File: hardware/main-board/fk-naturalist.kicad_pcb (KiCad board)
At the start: 2 copper layers, 91.8 x 37 mm, 131 parts, among them J1 Conn_01x07, J10 S2B-PH-SM4-TB, J11 RF-SMA-EDGE, J4 Conn_01x02, J5 Conn_01x03, J6 Conn_01x05, J7 CONN-HDR-2x5, J8 Conn_01x09, J9 MICRO-USB, M1 MOUNT_HOLE, M10 FIDUCIAL, M11 FIDUCIAL, M2 FIDUCIAL, M3 MOUNT_HOLE, M4 MOUNT_HOLE, M5 FIDUCIAL, M6 MOUNT_HOLE, M7 MICROSD, M8 FIDUCIAL, M9 FIDUCIAL, Q1 2N7002LT1G, Q2 2N7002LT1G, Q3 2N7002LT1G, Q4 2N7002LT1G, Q5 2N7002LT1G, SW1 SPNO, SW2 SPNO, U1 ATWINC1500-MR210PA, U10 FGPMMOPA6H, U103 BNO055, U11 MAX1704XX, U2 ATSAMD21G18A-AU, U4 24AA02E64, U5 S25FL116K0XMFI041, U6 BQ24074RGTT, U7 PCF8523, U8 MCP1700T-3302E/MB, U9 ISL8541x, Y1 FC-135, Y101 FC-135, Y2 FC-135

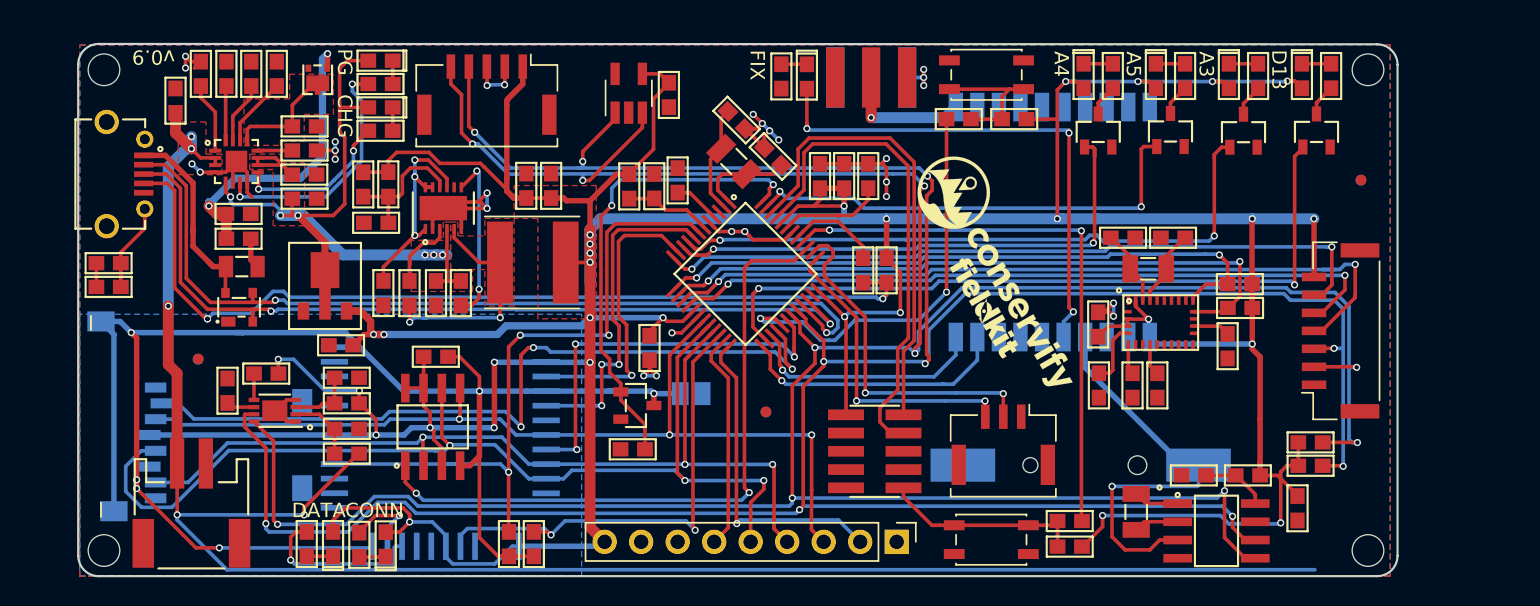
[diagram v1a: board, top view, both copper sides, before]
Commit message: Upgrade to Kicad 5. Add SK6812.
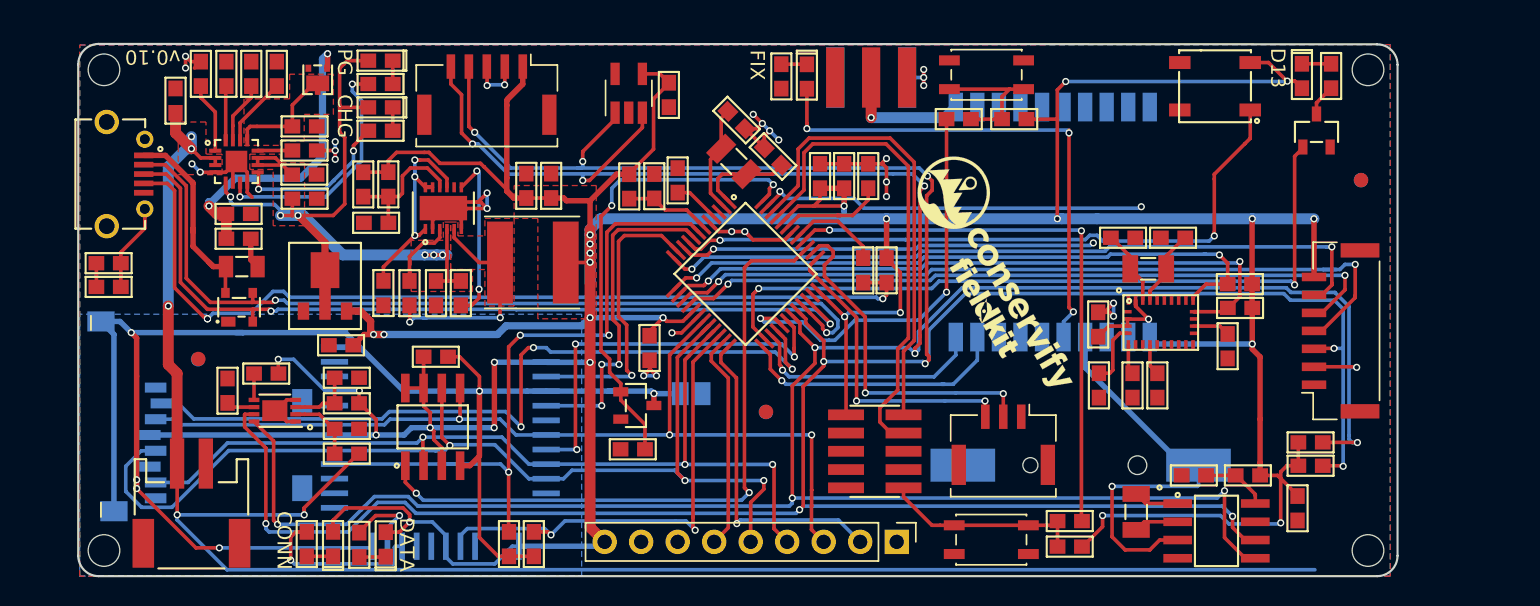
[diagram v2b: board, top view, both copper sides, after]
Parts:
- removed D4: Orange, RocketScreamKicadLibrary:LED-0603
- removed D5: Yellow, RocketScreamKicadLibrary:LED-0603
- removed D6: Blue, RocketScreamKicadLibrary:LED-0603
- removed Q2, Q3, Q4: 2N7002LT1G, RocketScreamKicadLibrary:SOT-23
- removed R18, R19, R20: 2K2, RocketScreamKicadLibrary:RES-0603
- added U3: SK6812, conservify:SK6812, F.Cu at (156.5, 112.7)
- C1, C10, C105, C106, C107, C108, C11, C12, C14, C18, C19, C20, C21, C22, C23, C24, C25, C26, C27, C28, C29, C3, C30, C31, C32, C4, C5, C6, C7, C8, C9: footprint RocketScreamKicadLibrary:CAP-0603 -> conservify:CAP-0603
- D1, D10, D11, D2, D3, D9: footprint RocketScreamKicadLibrary:LED-0603 -> conservify:LED-0603
- D7: footprint RocketScreamKicadLibrary:SOT-1016 -> conservify:SOT-1016
- D8: footprint RocketScreamKicadLibrary:SOT-143B -> conservify:SOT-143B
- F1: footprint RocketScreamKicadLibrary:MF-PSMF020X -> conservify:MF-PSMF020X
- J10: footprint RocketScreamKicadLibrary:S2B-PH-SM4-TB -> conservify:S2B-PH-SM4-TB
- J11: footprint RocketScreamKicadLibrary:RF-SMA-EDGE -> conservify:RF-SMA-EDGE
- J8: footprint Socket_Strips:Socket_Strip_Straight_1x09_Pitch2.54mm -> conservify:Socket_Strip_Straight_1x09_Pitch2.54mm
- L1, L2: footprint RocketScreamKicadLibrary:IND-0603 -> conservify:IND-0603
- M1, M3, M4, M6: footprint RocketScreamKicadLibrary:HOLE_NPTH_2.2MM -> conservify:HOLE_NPTH_2.2MM
- M10, M11, M2, M5, M8, M9: footprint Fiducials:Fiducial_0.75mm_Dia_1.5mm_Outer -> conservify:FIDUCIAL-1MM
- Q1, Q5: footprint RocketScreamKicadLibrary:SOT-23 -> conservify:SOT-23
- R1, R10, R101, R102, R103, R17, R2, R21, R22, R23, R24, R25, R26, R27, R3, R30, R31, R32, R33, R34, R35, R36, R37, R38, R39, R4, R40, R41, R42, R43, R44, R45, R5, R6, R8, R9: footprint RocketScreamKicadLibrary:RES-0603 -> conservify:RES-0603
- U11: footprint Housings_DFN_QFN:DFN-8-1EP_3x2mm_Pitch0.5mm -> conservify:DFN-8-1EP_3x2mm_Pitch0.5mm
- U2: footprint RocketScreamKicadLibrary:TQFP-48_7x7mm_Pitch0.5mm -> conservify:TQFP-48_7x7mm_Pitch0.5mm
- U4: footprint TO_SOT_Packages_SMD:SOT-23-5_HandSoldering -> conservify:SOT-23-5_HandSoldering
- U5, U7: footprint RocketScreamKicadLibrary:SOIC-8-N -> conservify:SOIC-8-N
- U6: footprint RocketScreamKicadLibrary:QFN-16_3x3mm -> conservify:QFN-16_3x3mm
- U8: footprint RocketScreamKicadLibrary:SOT-89 -> conservify:SOT-89
- U9: footprint Housings_DFN_QFN:DFN-12-1EP_3x4mm_Pitch0.5mm -> conservify:DFN-12-1EP_3x4mm_Pitch0.5mm
- Y1, Y101, Y2: footprint RocketScreamKicadLibrary:ABS07 -> conservify:ABS07
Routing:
- net /A4: track 36.9 -> 29.2 mm
- net /A5: track 32.3 -> 27.1 mm
- net /A3: track 44.4 -> 47.3 mm
- net Net-(Q2-Pad3): track 2.23 -> 0.00 mm
- net Net-(Q3-Pad3): track 2.21 -> 0.00 mm
- net Net-(Q4-Pad3): track 2.18 -> 0.00 mm
- net Net-(D6-Pad1): track 2.03 -> 0.00 mm
- net Net-(D5-Pad1): track 2.03 -> 0.00 mm
- net Net-(D4-Pad1): track 2.03 -> 0.00 mm
- net 3V3: track 365.4 -> 364.2 mm, vias 31 -> 29
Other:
- board text added: "v0.10"
- board text removed: "A3"
- board text removed: "A4"
- board text removed: "A5"
- board text removed: "v0.9"

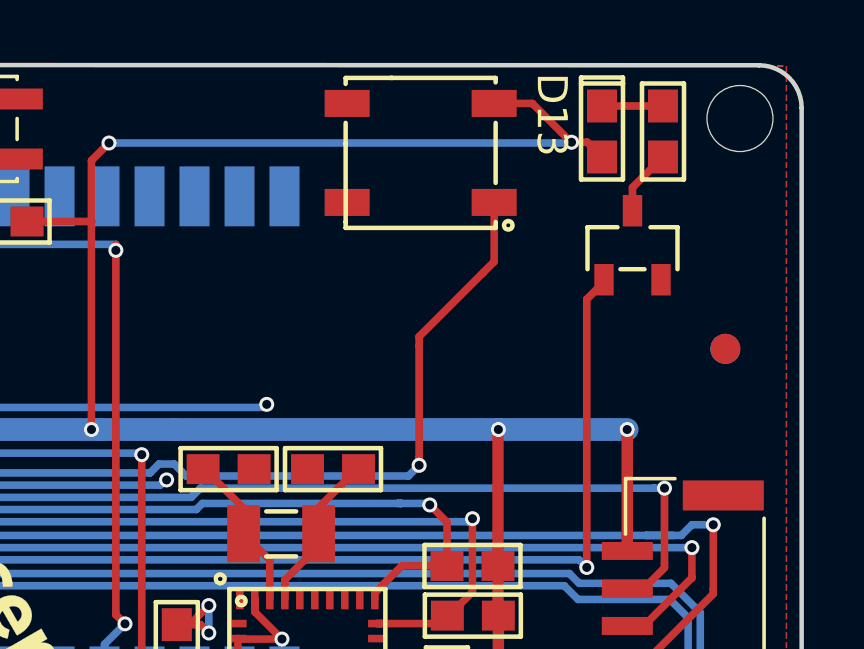
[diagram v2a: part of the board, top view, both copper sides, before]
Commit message: Fix SK6812.
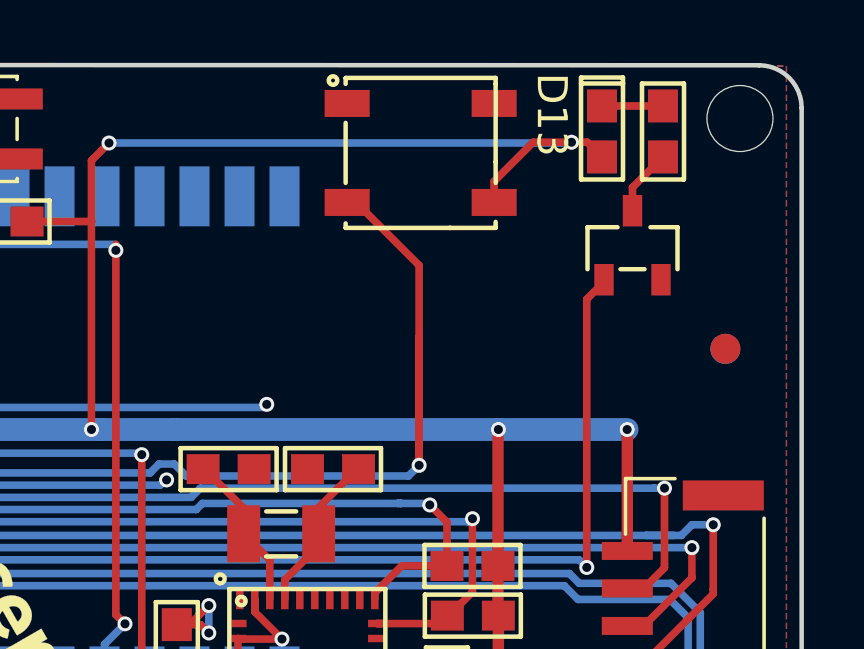
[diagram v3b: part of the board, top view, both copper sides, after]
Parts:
- BT1: value Battery_Cell -> BATTERY_CELL
- J7: value CONN-HDR-2x5 -> CONN_02x05_SWD; footprint conservify:HDR_2x5_Pitch1.27mm_SMD_JTAG_SWD -> conservify:HDR_02x05_Pitch1.27mm_SMD_SWD
- R1, R2, R38, R44: value 100k -> 100K
- R37, R39, R4, R40, R5: value 1k -> 1K
- turned U3 to 180 degrees
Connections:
- U3 pad 1: /A3 -> Net-(U3-Pad1)
- U3 pad 2: 3V3 -> /A3
- U3 pad 3: Net-(U3-Pad3) -> 3V3
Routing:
- net /A3: track 47.3 -> 51.7 mm
- net 3V3: track 364.2 -> 364.9 mm

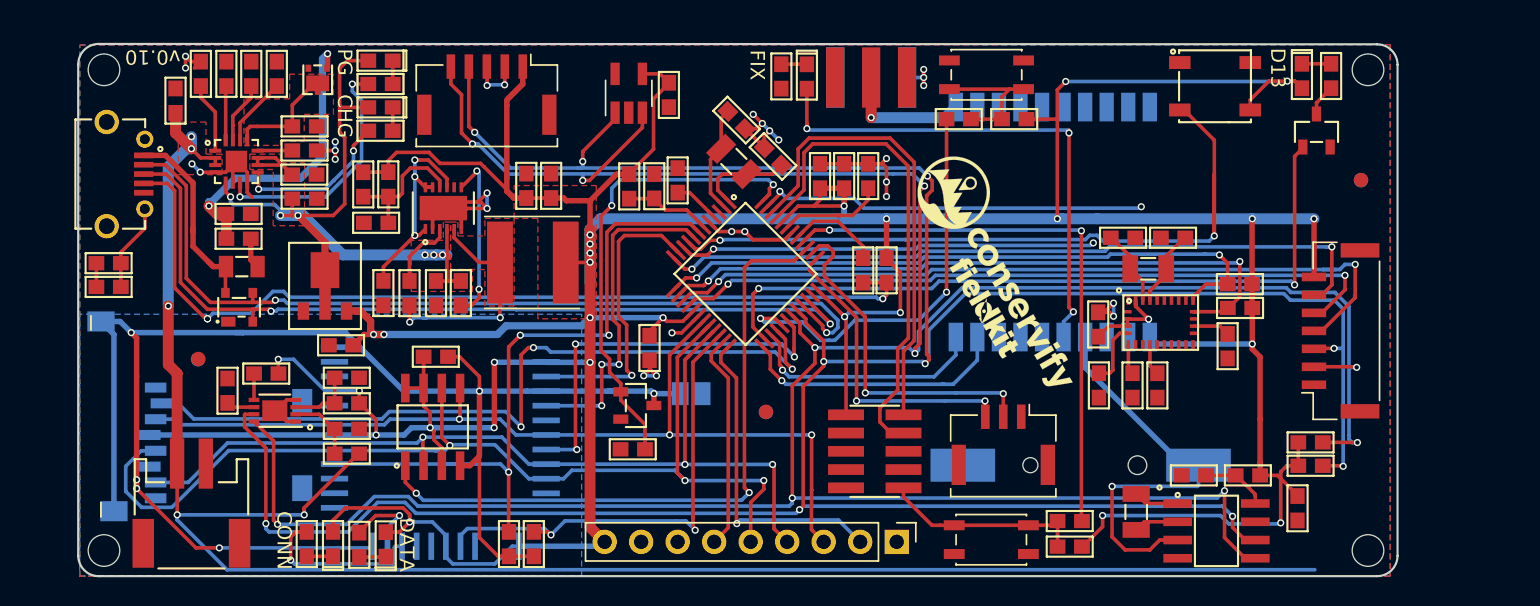
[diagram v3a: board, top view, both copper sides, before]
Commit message: Main board is now same as fk-core.
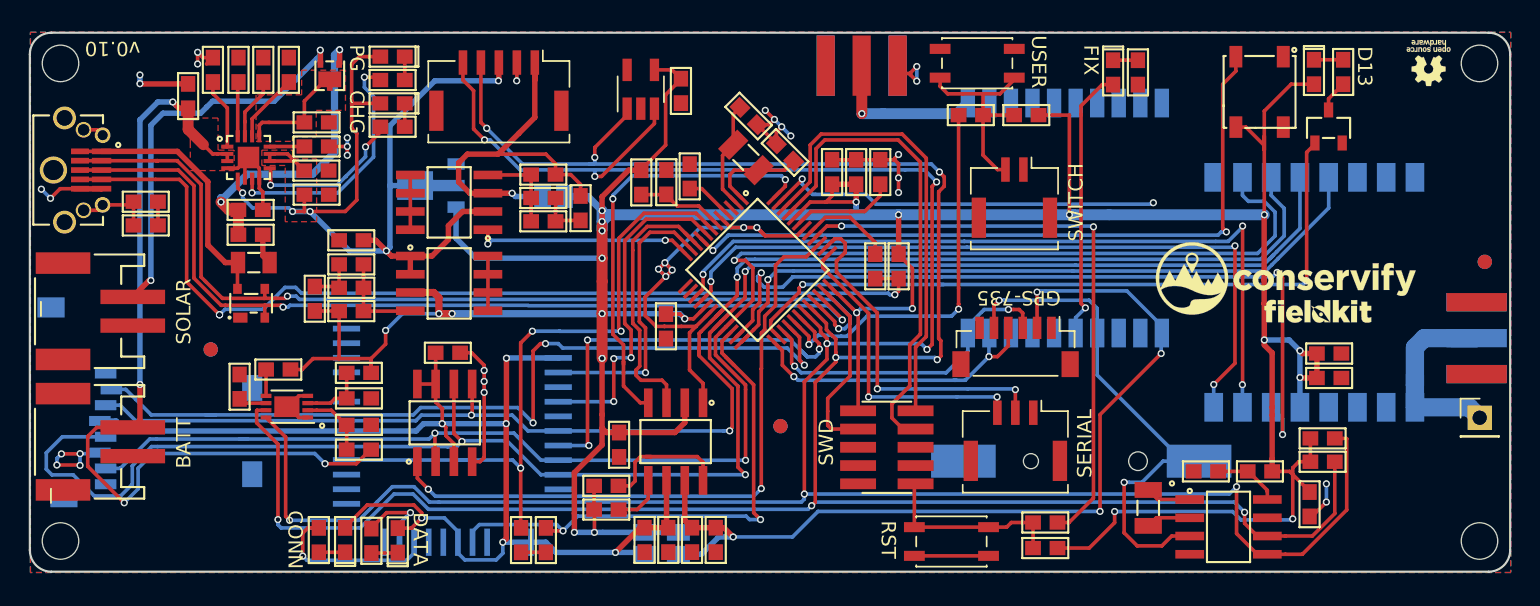
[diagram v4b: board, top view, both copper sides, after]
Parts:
- removed C105, C107: 22pF, conservify:CAP-0603
- removed C106, C108: 100nF, conservify:CAP-0603
- removed C31, C32: 10uF, conservify:CAP-0603
- removed the G*** at (140.5, 128.1)
- removed the G*** at (141.5, 125.8)
- removed the G*** at (161.2, 128.6)
- removed the G*** at (163.7, 129.0)
- removed L5: 22uH, conservify:WURTH_L_6.0x6.0
- removed M1, M3, M4, M6: MOUNT_HOLE, conservify:HOLE_NPTH_2.2MM
- removed Q5: 2N7002LT1G, conservify:SOT-23
- removed R101, R102, R103: 10K, conservify:RES-0603
- removed R26, R27: 4.7K, conservify:RES-0603
- removed R38, R44: 100K, conservify:RES-0603
- removed R45: 22K1, conservify:RES-0603
- removed U103: BNO055, conservify:BNO055
- removed Y101: FC-135, conservify:ABS07
- added C13: 100nF, conservify:CAP-0603, F.Cu at (164.4, 131.3)
- added C15: 100nF, conservify:CAP-0603, F.Cu at (115.0, 137.7)
- added C16: 100nF, conservify:CAP-0603, F.Cu at (120.1, 144.3)
- added C17: 10uF, conservify:CAP-0603, F.Cu at (121.7, 144.3)
- added C2: 47uF, conservify:CAP-0603, F.Cu at (164.4, 133.0)
- added C33: 100nF, conservify:CAP-0603, F.Cu at (116.8, 144.3)
- added C34: 10uF, conservify:CAP-0603, F.Cu at (118.4, 144.3)
- added G***: LOGO, conservify:fk_negative_2500, F.Cu at (163.6, 128.4)
- added G***: LOGO, conservify:conservify_text_negative_4000, F.Cu at (161.4, 126.1)
- added G***: LOGO, conservify:logo_osh_negative_3000, F.Cu at (171.3, 111.1)
- added J12: Conn_01x02, conservify:SJ_OPEN, B.Cu at (119.1, 144.5)
- added J13: CONN_01x06, conservify:JST_SH_BM06B-SRSS-TB_1x06-1MP_P1.00mm_Vertical, F.Cu at (142.6, 130.9)
- added J14: Conn_01x02, conservify:SJ_OPEN, B.Cu at (110.4, 120.4)
- added J2: Conn_01x02, conservify:SJ_OPEN, B.Cu at (116.8, 144.5)
- added J3: S2B-PH-SM4-TB, conservify:S2B-PH-SM4-TB, F.Cu at (78.9, 128.4)
- added R11: 100K, conservify:RES-0603, F.Cu at (96.4, 128.4)
- added R12: 165.7K, conservify:RES-0603, F.Cu at (96.4, 125.1)
- added R13: 100K, conservify:RES-0603, F.Cu at (109.7, 118.9)
- added R14: 165.7K, conservify:RES-0603, F.Cu at (109.7, 122.1)
- added R7: 10K, conservify:RES-0603, F.Cu at (114.1, 142.2)
- added REF**: HOLE_NPTH_2.54MM, conservify:HOLE_NPTH_2.54MM, F.Cu at (174.9, 111.1)
- added REF**: HOLE_NPTH_2.54MM, conservify:HOLE_NPTH_2.54MM, F.Cu at (76.1, 111.1)
- added REF**: HOLE_NPTH_2.54MM, conservify:HOLE_NPTH_2.54MM, F.Cu at (76.1, 144.4)
- added REF**: HOLE_NPTH_2.54MM, conservify:HOLE_NPTH_2.54MM, F.Cu at (174.9, 144.4)
- added U12: TPS2052B, conservify:SOIC-8-N, F.Cu at (118.9, 137.4)
- added U13: SK6812, conservify:SK6812, F.Cu at (159.6, 113.1)
- added U14: MCP1700T-3302E/MB, conservify:SOT-89, B.Cu at (101.9, 119.6)
- C23, C29: value 1uF -> 470pF
- C25: value 4.7uF -> 2.2uF
- C26: value 100nF -> 1uF
- C30: value 100pF -> 2.2uF
- J1: value Conn_01x07 -> RF-SMA-EDGE; footprint conservify:Molex_CLIK-Mate_502386-0770_1x07_P1.25mm_Horizontal -> conservify:RF-SMA-EDGE; moved to B.Cu
- J4: value Conn_01x02 -> Conn_01x01; footprint conservify:SJ_OPEN -> conservify:Socket_Strip_Straight_1x01_Pitch2.54mm; moved to F.Cu
- J5: value Conn_01x03 -> CONN_01x03_SERIAL
- J8: value Conn_01x09 -> CONN_01x02; footprint conservify:Socket_Strip_Straight_1x09_Pitch2.54mm -> conservify:Molex_CLIK-Mate_502382-0270_1x02_P1.25mm_Vertical
- U3: value SK6812 -> RFM95W; footprint conservify:SK6812 -> conservify:RFM9xW; moved to B.Cu
- U8: value MCP1700T-3302E/MB -> TL5209; footprint conservify:SOT-89 -> conservify:SOIC-8-N
- U9: value ISL8541x -> TL5209; footprint conservify:DFN-12-1EP_3x4mm_Pitch0.5mm -> conservify:SOIC-8-N
- moved M8 80.9 mm to (86.6, 131.0)
- moved J4 54.9 mm to (174.9, 135.8)
- moved M5 51.1 mm to (175.2, 124.9)
- moved M11 40.8 mm to (126.2, 136.4)
- moved M2 40.8 mm to (126.2, 136.4)
- moved M10 38.9 mm to (86.6, 131.0)
- moved J8 25.3 mm to (142.5, 120.5), turned to 180 degrees
- moved R39 24.8 mm to (151.1, 111.8)
- moved D11 21.3 mm to (149.4, 111.8)
- moved U3 15.9 mm to (163.4, 127.1), turned to 270 degrees
- moved C30 15.2 mm to (112.3, 121.2), turned to 270 degrees
- moved C29 12.9 mm to (109.7, 120.5), turned to 0 degrees
- moved M9 10.3 mm to (175.2, 124.9)
- moved J1 9.48 mm to (174.7, 130.3), turned to 0 degrees
- moved U8 8.64 mm to (103.2, 126.4)
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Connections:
- net /FLASH_CS renamed /D26_FLASH_CS
- net /SD_CS renamed /D12_SD_CS
- net /USER_SW renamed /D6_USER_SW
- net /WIFI_CS renamed /D7_WIFI_CS
- net /WIFI_EN renamed /D2_WIFI_EN
- net /WIFI_IRQ renamed /A2_WIFI_IRQ
- net /WIFI_RST renamed /A1_WIFI_RST
- net /WIFI_WAKE renamed /D8_WIFI_WAKE
- net AREF renamed Net-(C1-Pad1)
- C18 pad 1: 3V3 -> /PERIPH_3V3
- C18 pad 2: /PERIPH_GND -> GND
- C23 pad 1: 3V3 -> Net-(C23-Pad1)
- C25 pad 1: VBUS -> 3V3
- C26 pad 1: Net-(C26-Pad1) -> VBUS
- C26 pad 2: /ISL_VIN -> GND
- C30 pad 1: Net-(C30-Pad1) -> /MODULE_3V3
- C30 pad 2: 3V3 -> GND
- D2 pad 2: 3V3 -> /PERIPH_3V3
- D3 pad 2: 3V3 -> /PERIPH_3V3
- J1 pad 1: GND -> Net-(J1-Pad1)
- J1 pad 2: /SDA -> GND
- J1 pad 3: /SCL -> GND
- J1 pad 4: /I2S_BCLK -> GND
- J1 pad 5: /I2S_WS -> GND
- J4 pad 1: /PERIPH_GND -> Net-(J1-Pad1)
- J6 pad 1: 3V3 -> /MODULE_3V3
- J6 pad 3: GND -> VBUS
- J8 pad 1: /RADIO_RST -> GND
- J8 pad 2: /RADIO_CS -> Net-(J8-Pad2)
- M7 pad 4: 3V3 -> /PERIPH_3V3
- M7 pad 6: /PERIPH_GND -> GND
- M7 pad MT1: /PERIPH_GND -> GND
- M7 pad MT2: /PERIPH_GND -> GND
- R1 pad 2: /PERIPH_GND -> GND
- R10 pad 2: Net-(R10-Pad2) -> Net-(J8-Pad2)
- R17 pad 2: Net-(R10-Pad2) -> Net-(J8-Pad2)
- R2 pad 2: /PERIPH_GND -> GND
- R6 pad 1: /PERIPH_ENABLE -> Net-(R6-Pad1)
- R6 pad 2: GND -> 3V3
- SW2 pad 2: Net-(R10-Pad2) -> Net-(J8-Pad2)
- U1 pad 10: 3V3 -> /PERIPH_3V3
- U1 pad 12: /PERIPH_GND -> GND
- U1 pad 20: 3V3 -> /PERIPH_3V3
- U1 pad 23: 3V3 -> /PERIPH_3V3
- U1 pad 28: /PERIPH_GND -> GND
- U1 pad 9: /PERIPH_GND -> GND
- U10 pad 1: 3V3 -> /GPS_3V3
- U2 pad 10: /A4 -> /A4_GPS_EN
- U2 pad 12: /I2S_DATA -> /D9_MODULE_EN
- U2 pad 15: /I2S_BCLK -> /D1_RADIO_D1
- U2 pad 16: /I2S_WS -> /D0_RADIO_D2
- U2 pad 23: /RADIO_D0 -> /D2_RADIO_D0
- U2 pad 24: /RADIO_CS -> /D5_RADIO_CS
- U2 pad 48: /PERIPH_ENABLE -> /PERIPH_EN
- U3 pad 1: Net-(U3-Pad1) -> GND
- U3 pad 2: /A3 -> /MISO
- U3 pad 3: 3V3 -> /MOSI
- U3 pad 4: Net-(U3-Pad4) -> /SCK
- U5 pad 3: 3V3 -> /PERIPH_3V3
- U5 pad 4: /PERIPH_GND -> GND
- U5 pad 7: 3V3 -> /PERIPH_3V3
- U5 pad 8: 3V3 -> /PERIPH_3V3
- U8 pad 1: GND -> VBUS
- U9 pad 1: Net-(C29-Pad1) -> /D9_MODULE_EN
- U9 pad 2: GND -> VBUS
- U9 pad 3: Net-(C26-Pad1) -> /MODULE_3V3
- U9 pad 4: VBUS -> Net-(C29-Pad1)
- U9 pad 5: /ISL_VIN -> GND
- U9 pad 7: Net-(R38-Pad1) -> GND
- U9 pad 8: Net-(U9-Pad8) -> GND
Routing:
- net /PERIPH_GND: track 108.8 -> 0.00 mm, vias 6 -> 0
- net /PERIPH_3V3: track 0.00 -> 89.5 mm, vias 0 -> 6
- net 3V3: track 364.9 -> 275.5 mm, vias 29 -> 23
- net GND: track 66.7 -> 133.9 mm, vias 28 -> 34
- net VBAT: track 128.5 -> 62.0 mm, vias 5 -> 4
- net /GPS_3V3: track 0.00 -> 64.3 mm, vias 0 -> 4
- net /D2_RADIO_D0: track 0.00 -> 58.5 mm, vias 0 -> 3
- net /I2S_BCLK: track 54.8 -> 0.00 mm, vias 2 -> 0
- net /D1_RADIO_D1: track 0.00 -> 53.4 mm, vias 0 -> 3
- net /D0_RADIO_D2: track 0.00 -> 51.4 mm, vias 0 -> 3
- net /I2S_DATA: track 51.0 -> 0.00 mm, vias 2 -> 0
- net /I2S_WS: track 50.4 -> 0.00 mm, vias 2 -> 0
- net /SCK: track 74.5 -> 124.8 mm
- net /D5_RADIO_CS: track 0.00 -> 49.1 mm, vias 0 -> 1
- net /MISO: track 64.6 -> 112.0 mm
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- removed copper zone on F.Cu, net /ISL_VIN
- removed copper zone on B.Cu, net /PERIPH_GND
- removed copper zone on F.Cu, net 3V3
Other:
- board size 91.8 x 37 mm -> 103 x 37.5 mm
- board text added: "BATT"
- board text added: "GPS-735"
- board text added: "GPS_3V3"
- board text added: "MODULE_3V3"
- board text added: "PERIPH_3V3"
- board text added: "RST"
- board text added: "SERIAL"
- board text added: "SOLAR"
- board text added: "SWD"
- board text added: "SWITCH"
- board text added: "USER"
